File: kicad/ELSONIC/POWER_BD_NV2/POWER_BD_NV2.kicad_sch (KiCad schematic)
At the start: 0 parts

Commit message: Initial commit with all embedded projects
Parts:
- added C1: CR1201, symbol 04_MyLib_Passive:CR1201
- added C2, C3: DS222M_250VAC, symbol 04_MyLib_Passive:C
- added C4: C_Pol, symbol 04_MyLib_Passive:C_Pol
- added C5: CC472_630V, symbol 04_MyLib_Passive:C
- added D1: GBJ406, GBL406BPC01HF, symbol 03_MyLib_Active:GBL406
- added D2: UF4007, DIOAD1530W84L490D260, symbol 04_MyLib_Passive:UF4007
- added F1: SR5_2.5A, SR525ABK, symbol 05_MyLib_Device:SR525A
- added H3: F_GND, symbol Mechanical:MountingHole_Pad
- added IC1: ICE3BR0665JXKLA1, DIP788W56P254L944H480Q8N, symbol 01_MyLib_ICs:ICE3BR0665JXKLA1
- added J1: SMW250-02P, 02_MyFoot_Connectors:SMW25002, symbol 02_MyLib_Connectors:SMW250-02P
- added J2: SMW250-06P, 02_MyFoot_Connectors:SMW25006, symbol 02_MyLib_Connectors:SMW250-06P
- added J3, J5, L1, N1: TAP_250, symbol 02_MyLib_Connectors:TAP_250
- added LF1: LF1140_602, symbol 04_MyLib_Passive:LF1140-602
- added R1: 560K_1W, symbol 04_MyLib_Passive:R
- added R2: 56K_2W, symbol 04_MyLib_Passive:R
- added RV1: TNR_14D471, MOV14D471K, symbol 04_MyLib_Passive:MOV-14D471
- added TR1: EER28, symbol 04_MyLib_Passive:EER28
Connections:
- new net: C1.1, F1.1, N1.1 (Pin_1), N1.2 (Pin_2)
- new net: C2.2, F1.2, LF1.2, R1.2, RV1.2
- new net: C1.2, C3.1, L1.1 (Pin_1), L1.2 (Pin_2), LF1.1, R1.1, RV1.1
- new net: C4.1, D1.1 (+)
- new net: D1.2, LF1.3
- new net: D1.3, LF1.4
- new net GNDPWR: C2.1, C3.2, H3.1, J3.1 (Pin_1), J3.2 (Pin_2)

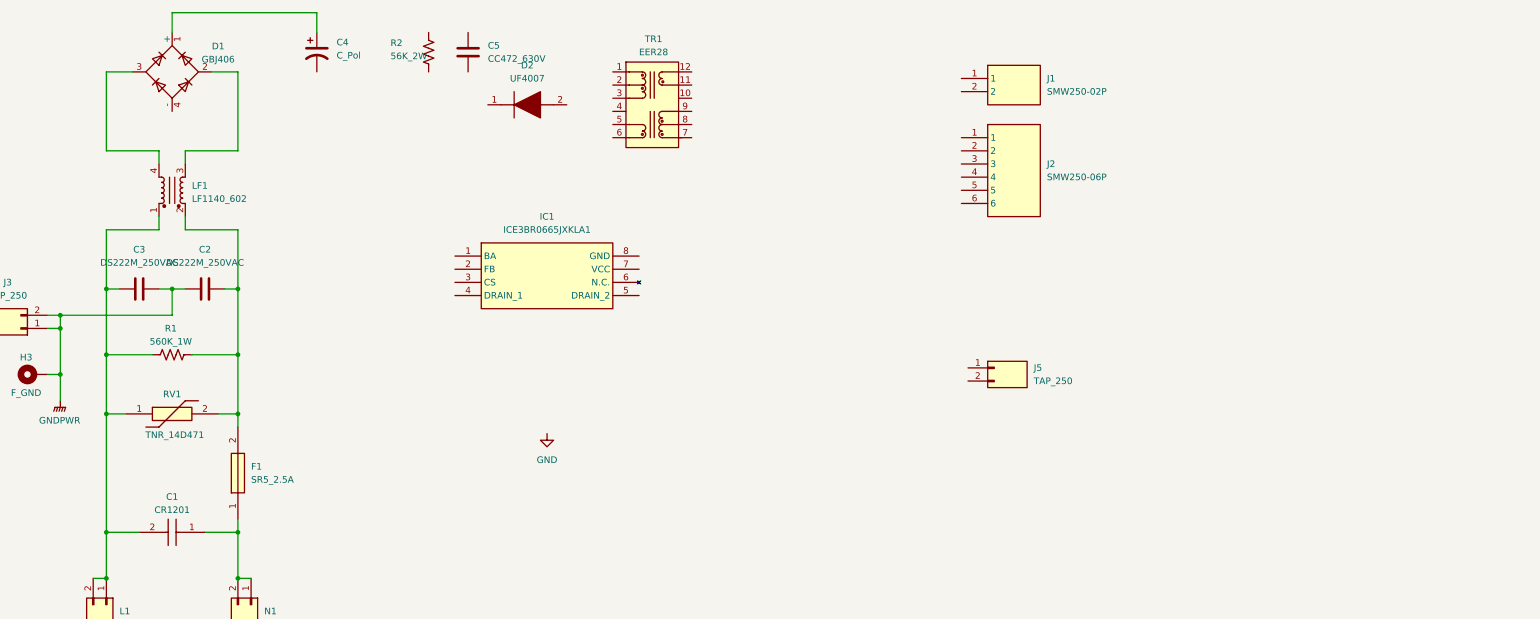
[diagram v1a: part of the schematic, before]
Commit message: Update KiCAD libraries: Add TL431 components and passive footprints
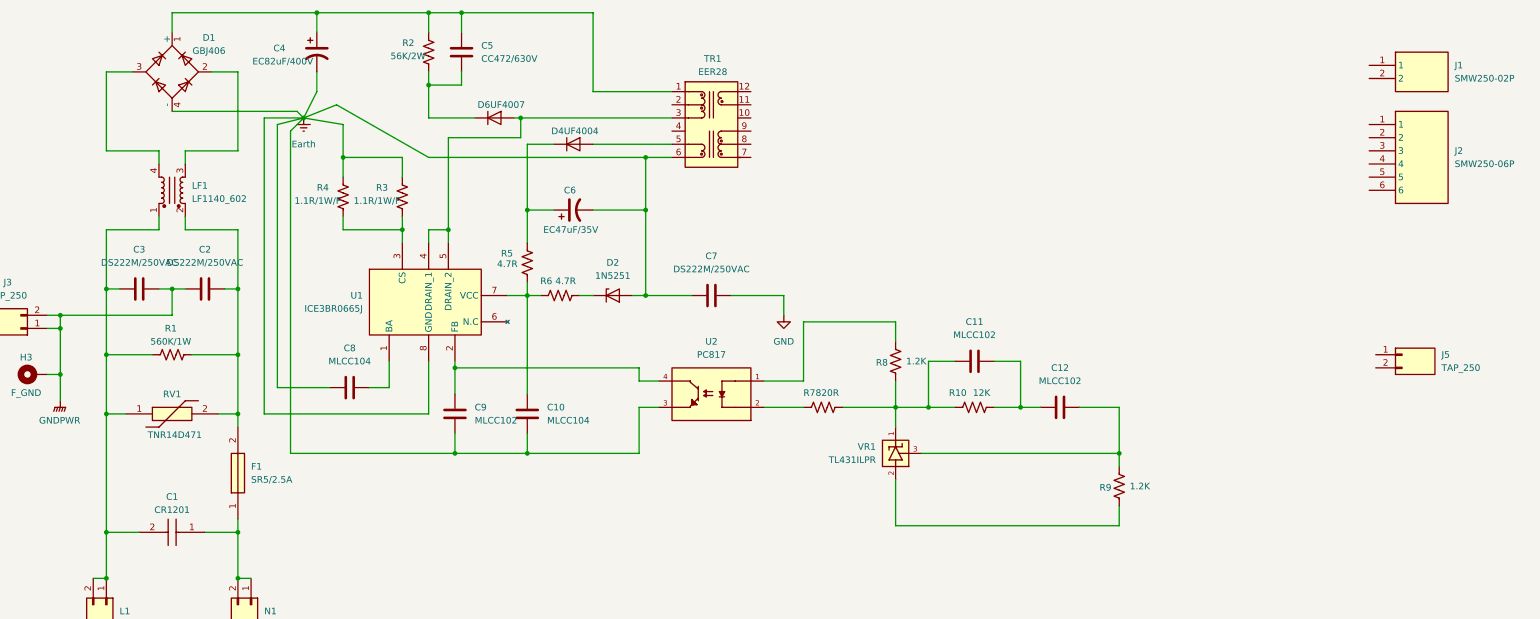
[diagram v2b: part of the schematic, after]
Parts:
- removed D2: UF4007, DIOAD1530W84L490D260, symbol 04_MyLib_Passive:UF4007
- removed IC1: ICE3BR0665JXKLA1, DIP788W56P254L944H480Q8N, symbol 01_MyLib_ICs:ICE3BR0665JXKLA1
- added C10, C8: MLCC104, symbol 04_MyLib_Passive:C
- added C11, C12, C9: MLCC102, symbol 04_MyLib_Passive:C
- added C6: EC47uF/35V, symbol 04_MyLib_Passive:C_Pol
- added C7: DS222M/250VAC, symbol 04_MyLib_Passive:C
- added D2: 1N5251, 03_MyFoot_Active:ZENER_0_5W_P7.62mm_Hori, symbol 03_MyLib_Active:1N5251
- added D4: UF4004, Diode_THT:D_DO-41_SOD81_P10.16mm_Horizontal, symbol 03_MyLib_Active:UF4004
- added D6: UF4007, Diode_THT:D_DO-41_SOD81_P10.16mm_Horizontal, symbol 03_MyLib_Active:UF4007
- added R10: 12K, 04_MyFoot_Passive:R_Axial_P10.16mm, symbol 04_MyLib_Passive:R
- added R3, R4: 1.1R/1W/F, symbol 04_MyLib_Passive:R
- added R5, R6: 4.7R, symbol 04_MyLib_Passive:R
- added R7: 820R, symbol 04_MyLib_Passive:R
- added R8: 1.2K, symbol 04_MyLib_Passive:R
- added R9: 1.2K, 04_MyFoot_Passive:R_Axial_P10.16mm, symbol 04_MyLib_Passive:R
- added U1: ICE3BR0665J, DIP788W56P254L944H480Q8N, symbol 01_MyLib_ICs:ICE3BR0665J
- added U2: PC817, DIP762W50P254L495H455Q4, symbol 01_MyLib_ICs:PC817X3NSZ1B
- added VR1: TL431ILPR, 03_MyFoot_Active:TO92250P470H770-3, symbol 01_MyLib_ICs:TL431ILPR
- C2, C3: value DS222M_250VAC -> DS222M/250VAC
- C4: value C_Pol -> EC82uF/400V
- C5: value CC472_630V -> CC472/630V
- F1: value SR5_2.5A -> SR5/2.5A
- R1: value 560K_1W -> 560K/1W
- R2: value 56K_2W -> 56K/2W
- RV1: value TNR_14D471 -> TNR14D471
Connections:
- net GND: now also C7.2
- net at C4.1, D1.1 (+): now also C5.1, R2.1, TR1.1 (P0)
- net Earth: now reaches D1.4 (-)
- net Earth: now also C4.2, TR1.6 (Vcc_GND), C10.1, C6.2, C7.1, C8.1, C9.1, D2.2 (A), R3.1, R4.1, U1.8 (GND), U2.3
- net at TR1.3 (P2): now also D6.2 (A), U1.4 (DRAIN_1), U1.5 (DRAIN_2)
- net at TR1.5 (Vcc): now also D4.2 (A)
- net at R2.2: now also C5.2, D6.1 (K)
- new net: C6.1, D4.1 (K), R5.1
- new net: C10.2, R5.2, R6.1, U1.7 (VCC)
- new net: D2.1 (K), R6.2
- new net: C11.2, C12.1, R10.2
- new net: C12.2, R9.2, VR1.3
- new net: C11.1, R10.1, R7.2, R8.1, VR1.1
- new net: R3.2, R4.2, U1.3 (CS)
- new net: C8.2, U1.1 (BA)
- new net: R9.1, VR1.2
- new net: C9.2, U1.2 (FB), U2.4
- new net: R7.1, U2.2
- new net: R8.2, U2.1
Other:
- moved on the sheet: C5, J1, J2, J5, TR1

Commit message: Update KiCAD schematic and library files
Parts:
- added C13, C14, C15: CC471/1kV, symbol 04_MyLib_Passive:C
- added C16, C17, C18: EC1000uF/25V, symbol 04_MyLib_Passive:C_Pol
- added D3, D5, D7: MUR1640FCT, 03_MyFoot_Active:TO255P510X1070X2140-3P, symbol 03_MyLib_Active:MUR1640FCT
- added L2: Inductor, symbol 04_MyLib_Passive:Inductor
- added R11: 220R, 04_MyFoot_Passive:R_Axial_P10.16mm, symbol 04_MyLib_Passive:R
- added R12: 10K, 04_MyFoot_Passive:R_Axial_P10.16mm, symbol 04_MyLib_Passive:R
- added R13, R14, R15: 10R/1W, 04_MyFoot_Passive:R_Axial_P10.16mm, symbol 04_MyLib_Passive:R
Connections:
- net at C12.2, R9.2, VR1.3: now also R11.1
- net at TR1.8 (N1): now also D3.1 (A), D3.3 (A), R13.1
- net at R8.2, U2.1: now also R12.2
- new net: C13.2, C16.1, D3.2 (K)
- new net: R11.2, R12.1
- new net: C13.1, R13.2
- new net: C15.1, R15.2
- new net: C14.1, R14.2
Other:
- moved on the sheet: C11, C12, R10, R7, R8, R9, VR1

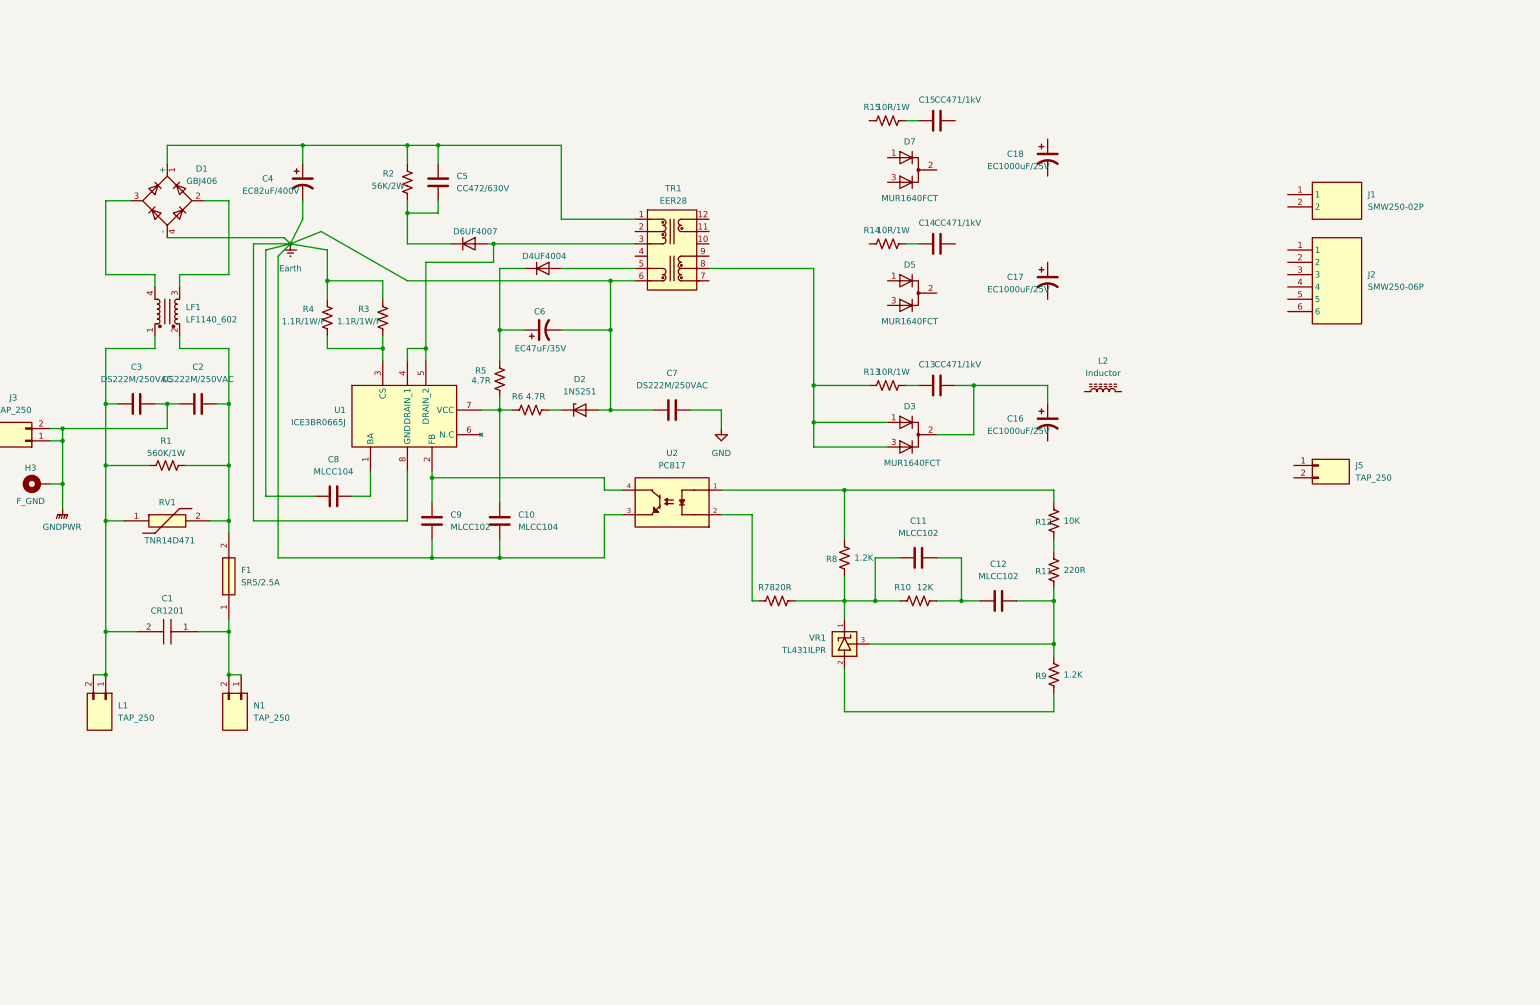
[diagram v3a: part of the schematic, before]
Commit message: Attiny85-Dimmer: ADC 보정 수정 및 main.cpp 업데이트
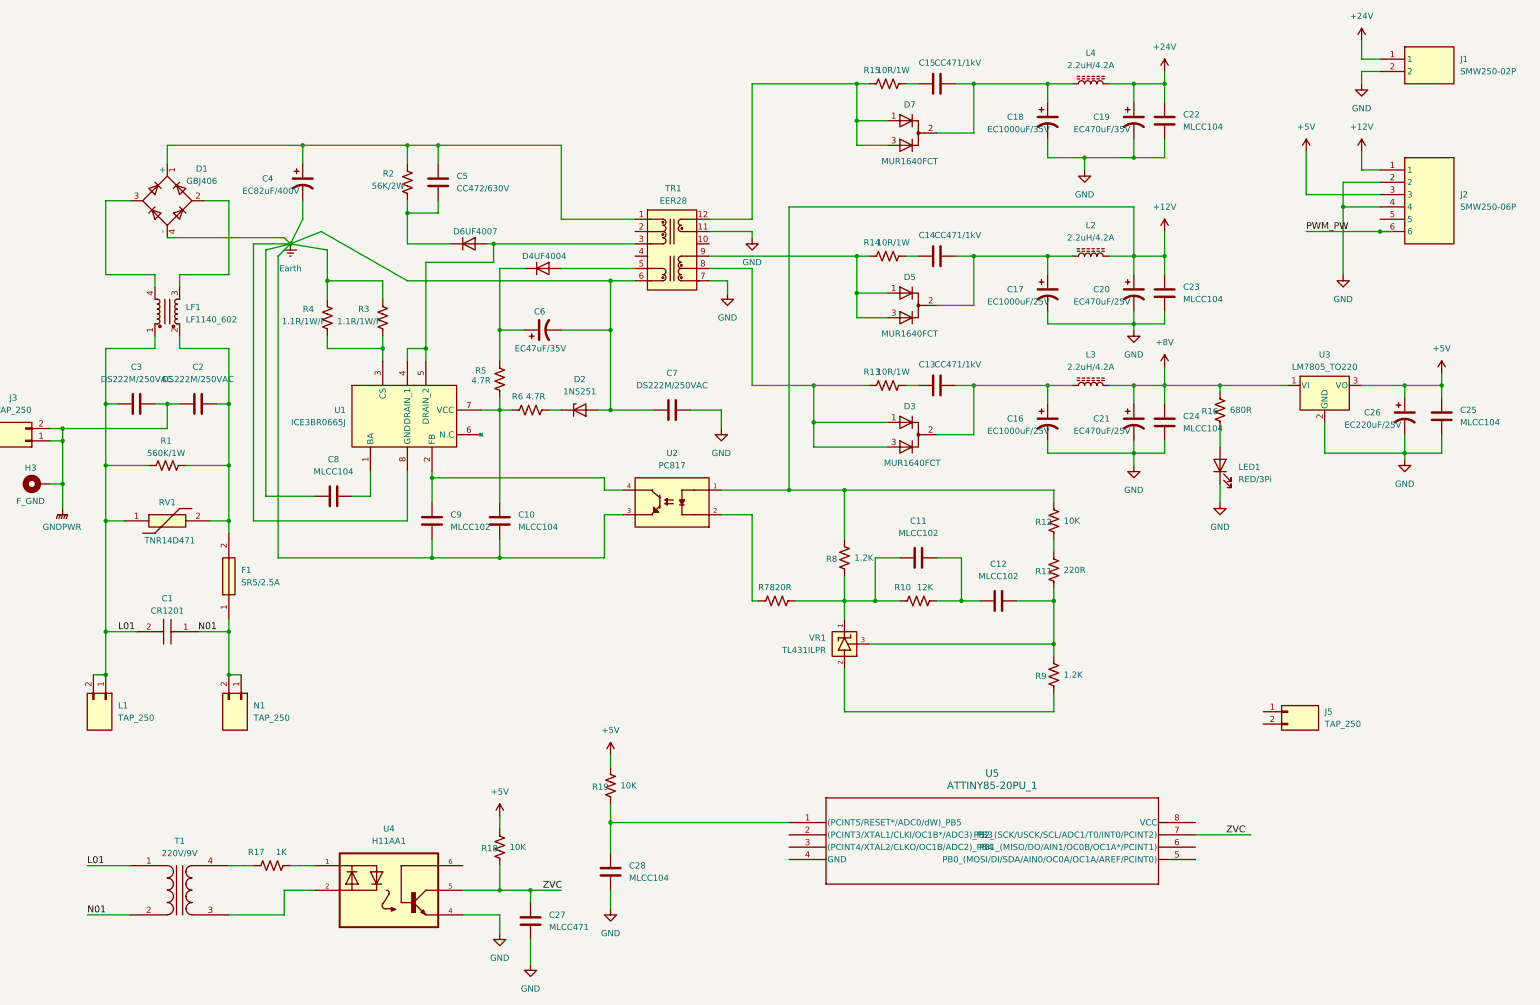
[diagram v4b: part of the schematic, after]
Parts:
- added C19: EC470uF/35V, symbol 04_MyLib_Passive:C_Pol
- added C20, C21: EC470uF/25V, symbol 04_MyLib_Passive:C_Pol
- added C22, C23, C24, C25, C28: MLCC104, symbol 04_MyLib_Passive:C
- added C26: EC220uF/25V, symbol 04_MyLib_Passive:C_Pol
- added C27: MLCC471, symbol 04_MyLib_Passive:C
- added L3, L4: 2.2uH/4.2A, symbol 04_MyLib_Passive:Inductor
- added LED1: RED/3Pi, symbol 03_MyLib_Active:LED
- added R16: 680R, 04_MyFoot_Passive:R_Axial_P10.16mm, symbol 04_MyLib_Passive:R
- added R17: 1K, symbol 04_MyLib_Passive:R
- added R18, R19: 10K, 04_MyFoot_Passive:R_Axial_P10.16mm, symbol 04_MyLib_Passive:R
- added T1: 220V/9V, symbol 04_MyLib_Passive:Transformer_1P_1S
- added U3: LM7805_TO220, Package_TO_SOT_THT:TO-220-3_Vertical, symbol 01_MyLib_ICs:LM7805_TO220
- added U4: H11AA1, DIP762W50P254L730H410Q6, symbol 01_MyLib_ICs:H11AA1
- added U5: ATTINY85-20PU_1, 8P3_ATM, symbol 00_MyLib_MCU:ATTINY85-20PU_1
- C18: value EC1000uF/25V -> EC1000uF/35V
- L2: value Inductor -> 2.2uH/4.2A
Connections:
- net GND: now also C16.2, C17.2, C18.2, J1.2, J2.2, J2.4, TR1.11 (N_GND2), TR1.7 (N_GND1), C19.2, C20.2, C21.2, C22.1, C23.1, C24.1, C25.1, C26.2, C27.1, C28.1, LED1.1 (K), U3.2 (GND), U4.4
- net at C18.1: now also C15.2, D7.2 (K), L4.1
- net at C13.2, C16.1, D3.2 (K): now also L3.1
- net N01: now reaches C1.1, F1.1, N1.1 (Pin_1), N1.2 (Pin_2)
- net N01: now also T1.2 (AB)
- net at D5.1 (A): now also D5.3 (A), R14.1, TR1.9 (N2)
- net at D5.2 (K): now also C14.2, C17.1, L2.1
- net L01: now reaches C1.2, C3.1, L1.1 (Pin_1), L1.2 (Pin_2), LF1.1, R1.1, RV1.1
- net L01: now also T1.1 (AA)
- net at R15.1: now also D7.1 (A), D7.3 (A), TR1.12 (N3)
- net +24V: now reaches J1.1
- net +24V: now also C19.1, C22.2, L4.2
- net +12V: now reaches J2.1
- net +12V: now also L2.2, R12.2, R8.2, U2.1, C20.1, C23.2
- net +5V: now reaches J2.3
- net +5V: now also C25.2, C26.1, R18.2, R19.2, U3.3 (VO)
- net PWM_PW: now reaches J2.6
- new net: C28.2, R19.1, U5.1 ((PCINT5/RESET*/ADC0/dW)_PB5)
- new net: R17.1, T1.4 (SB)
- new net: R17.2, U4.1
- new net: T1.3 (SA), U4.2
- new net: LED1.2 (A), R16.1
- new net +8V: C21.1, C24.2, L3.2, R16.2, U3.1 (VI)
- new net ZVC: C27.2, R18.1, U4.5, U5.7 (PB2_(SCK/USCK/SCL/ADC1/T0/INT0/PCINT2))
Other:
- moved on the sheet: C14, C15, C17, C18, D5, D7, J1, J2, J5, R14, R15
